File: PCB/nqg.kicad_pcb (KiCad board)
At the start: 2 copper layers, 214.3 x 81 mm, 78 parts, among them SW1 SW_PUSH, SW10 SW_PUSH, SW11 SW_PUSH, SW12 SW_PUSH, SW13 SW_PUSH, SW14 SW_PUSH, SW15 SW_PUSH, SW16 SW_PUSH, SW17 SW_PUSH, SW18 SW_PUSH, SW19 SW_PUSH, SW2 SW_PUSH, SW20 SW_PUSH, SW21 SW_PUSH, SW22 SW_PUSH, SW23 SW_PUSH, SW24 SW_PUSH, SW25 SW_PUSH, SW26 SW_PUSH, SW27 SW_PUSH, SW28 SW_PUSH, SW29 SW_PUSH, SW3 SW_PUSH, SW30 SW_PUSH, SW31 SW_PUSH, SW32 SW_PUSH, SW33 SW_PUSH, SW34 SW_PUSH, SW35 SW_PUSH, SW36 SW_PUSH, SW37 SW_PUSH, SW38 SW_PUSH, SW39 SW_PUSH, SW4 SW_PUSH, SW40 SW_PUSH, SW5 SW_PUSH, SW6 SW_PUSH, SW7 SW_PUSH, SW8 SW_PUSH, SW9 SW_PUSH, U1 ProMicro

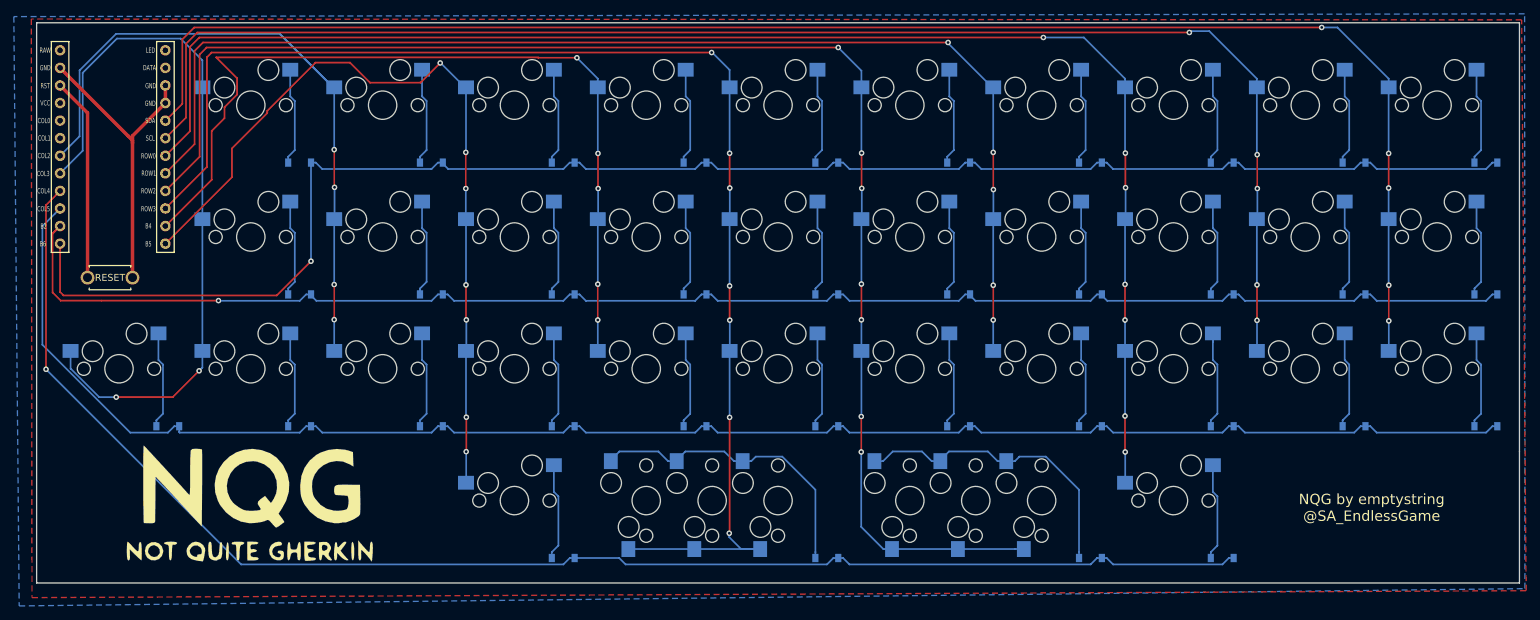
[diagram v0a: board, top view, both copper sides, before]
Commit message: added mounting holes
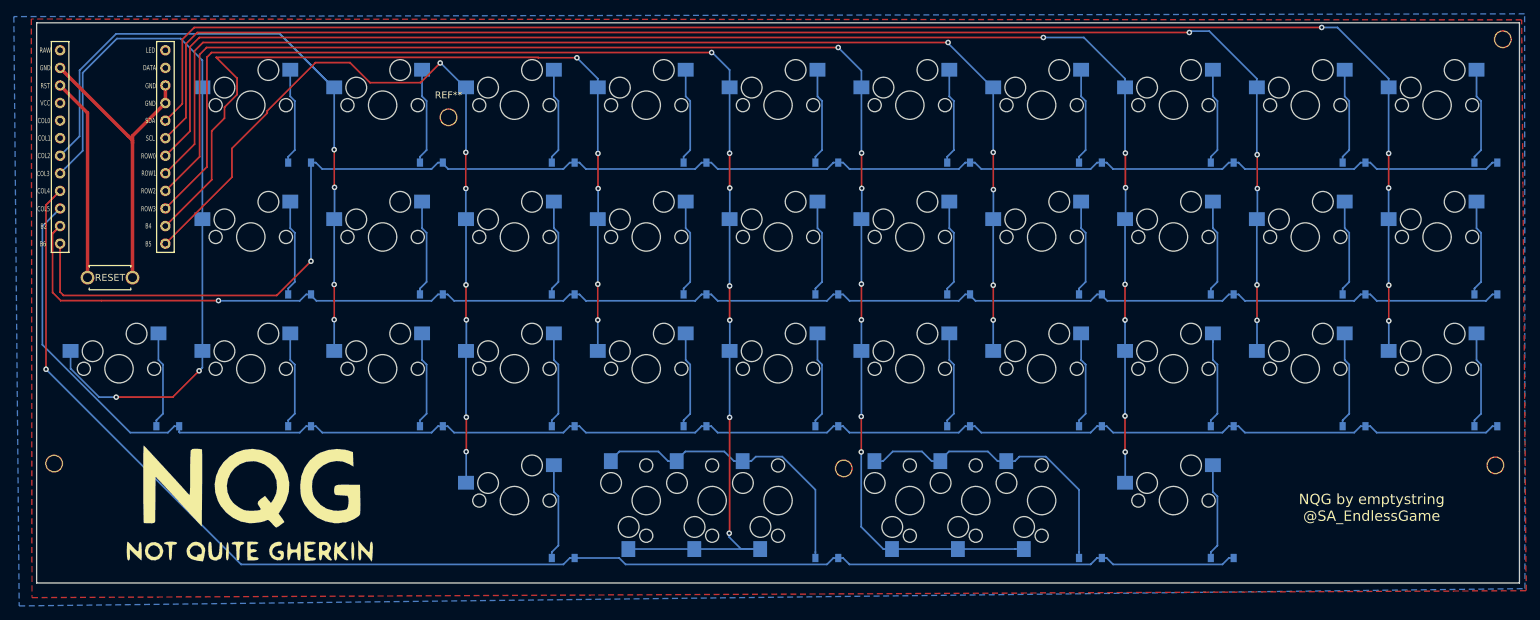
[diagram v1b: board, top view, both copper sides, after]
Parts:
- added ?: MountingHole_2.2mm_M2_Pad, MountingHole:MountingHole_2.2mm_M2_Pad, F.Cu at (143.0, 185.2)
- added ?: MountingHole_2.2mm_M2_Pad, MountingHole:MountingHole_2.2mm_M2_Pad, F.Cu at (351.3, 185.4)
- added ?: MountingHole_2.2mm_M2_Pad, MountingHole:MountingHole_2.2mm_M2_Pad, F.Cu at (257.1, 185.8)
- added ?: MountingHole_2.2mm_M2_Pad, MountingHole:MountingHole_2.2mm_M2_Pad, F.Cu at (352.4, 123.8)
- added REF**: MountingHole_2.2mm_M2_Pad, MountingHole:MountingHole_2.2mm_M2_Pad, F.Cu at (200.0, 135.1)
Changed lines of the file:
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@@
     (tracks 653)
     (zones 0)
-    (modules 78)
+    (modules 83)
     (nets 58)
   )
@@
     (mod_text_size 1 1)
     (mod_text_width 0.15)
-    (pad_size 1.524 1.524)
-    (pad_drill 0.762)
+    (pad_size 2.6 2.6)
+    (pad_drill 2.2)
     (pad_to_mask_clearance 0.051)
     (solder_mask_min_width 0.25)
@@
       (xy 17.963182 -1.693333) (xy 18.457333 -1.693333) (xy 18.457333 -4.741333)) (layer B.SilkS) (width 0.01))
   )
+  (module MountingHole:MountingHole_2.2mm_M2_Pad (layer F.Cu)
+    (at 143.025 185.15)
+    (descr "Mounting Hole 2.2mm, M2")
+    (tags "mounting hole 2.2mm m2")
+    (attr virtual)
+    (fp_text reference "" (at 0 -3.2) (layer F.SilkS)
+      (effects (font (size 1 1) (thickness 0.15)))
+    )
+    (fp_text value MountingHole_2.2mm_M2_Pad (at 0 3.2) (layer F.Fab)
+      (effects (font (size 1 1) (thickness 0.15)))
+    )
+    (fp_circle (center 0 0) (end 2.45 0) (layer F.CrtYd) (width 0.05))
+    (fp_circle (center 0 0) (end 2.2 0) (layer Cmts.User) (width 0.15))
+    (fp_text user %R (at 0.3 0) (layer F.Fab)
+      (effects (font (size 1 1) (thickness 0.15)))
+    )
+    (pad 1 thru_hole circle (at 0 0) (size 2.6 2.6) (drill 2.2) (layers *.Cu *.Mask))
+  )
+  (module MountingHole:MountingHole_2.2mm_M2_Pad (layer F.Cu)
+    (at 351.325 185.4)
+    (descr "Mounting Hole 2.2mm, M2")
+    (tags "mounting hole 2.2mm m2")
+    (attr virtual)
+    (fp_text reference "" (at 0 -3.2) (layer F.SilkS)
+      (effects (font (size 1 1) (thickness 0.15)))
+    )
+    (fp_text value MountingHole_2.2mm_M2_Pad (at 0 3.2) (layer F.Fab)
+      (effects (font (size 1 1) (thickness 0.15)))
+    )
+    (fp_circle (center 0 0) (end 2.45 0) (layer F.CrtYd) (width 0.05))
+    (fp_circle (center 0 0) (end 2.2 0) (layer Cmts.User) (width 0.15))
+    (fp_text user %R (at 0.3 0) (layer F.Fab)
+      (effects (font (size 1 1) (thickness 0.15)))
+    )
+    (pad 1 thru_hole circle (at 0 0) (size 2.6 2.6) (drill 2.2) (layers *.Cu *.Mask))
+  )
+  (module MountingHole:MountingHole_2.2mm_M2_Pad (layer F.Cu)
+    (at 257.15 185.85)
+    (descr "Mounting Hole 2.2mm, M2")
+    (tags "mounting hole 2.2mm m2")
+    (attr virtual)
+    (fp_text reference "" (at 0 -3.2) (layer F.SilkS)
+      (effects (font (size 1 1) (thickness 0.15)))
+    )
+    (fp_text value MountingHole_2.2mm_M2_Pad (at 0 3.2) (layer F.Fab)
+      (effects (font (size 1 1) (thickness 0.15)))
+    )
+    (fp_circle (center 0 0) (end 2.45 0) (layer F.CrtYd) (width 0.05))
+    (fp_circle (center 0 0) (end 2.2 0) (layer Cmts.User) (width 0.15))
+    (fp_text user %R (at 0.3 0) (layer F.Fab)
+      (effects (font (size 1 1) (thickness 0.15)))
+    )
+    (pad 1 thru_hole circle (at 0 0) (size 2.6 2.6) (drill 2.2) (layers *.Cu *.Mask))
+  )
+  (module MountingHole:MountingHole_2.2mm_M2_Pad (layer F.Cu)
+    (at 352.4 123.825)
+    (descr "Mounting Hole 2.2mm, M2")
+    (tags "mounting hole 2.2mm m2")
+    (attr virtual)
+    (fp_text reference "" (at 0 -3.2) (layer F.SilkS)
+      (effects (font (size 1 1) (thickness 0.15)))
+    )
+    (fp_text value MountingHole_2.2mm_M2_Pad (at 0 3.2) (layer F.Fab)
+      (effects (font (size 1 1) (thickness 0.15)))
+    )
+    (fp_circle (center 0 0) (end 2.45 0) (layer F.CrtYd) (width 0.05))
+    (fp_circle (center 0 0) (end 2.2 0) (layer Cmts.User) (width 0.15))
+    (fp_text user %R (at 0.3 0) (layer F.Fab)
+      (effects (font (size 1 1) (thickness 0.15)))
+    )
+    (pad 1 thru_hole circle (at 0 0) (size 2.6 2.6) (drill 2.2) (layers *.Cu *.Mask))
+  )
+  (module MountingHole:MountingHole_2.2mm_M2_Pad (layer F.Cu)
+    (at 200.025 135.1)
+    (descr "Mounting Hole 2.2mm, M2")
+    (tags "mounting hole 2.2mm m2")
+    (attr virtual)
+    (fp_text reference REF** (at 0 -3.2) (layer F.SilkS)
+      (effects (font (size 1 1) (thickness 0.15)))
+    )
+    (fp_text value MountingHole_2.2mm_M2_Pad (at 0 3.2) (layer F.Fab)
+      (effects (font (size 1 1) (thickness 0.15)))
+    )
+    (fp_circle (center 0 0) (end 2.45 0) (layer F.CrtYd) (width 0.05))
+    (fp_circle (center 0 0) (end 2.2 0) (layer Cmts.User) (width 0.15))
+    (fp_text user %R (at 0.3 0) (layer F.Fab)
+      (effects (font (size 1 1) (thickness 0.15)))
+    )
+    (pad 1 thru_hole circle (at 0 0) (size 2.6 2.6) (drill 2.2) (layers *.Cu *.Mask))
+  )
   (gr_text "NQG by emptystring\n@SA_EndlessGame" (at 333.45 191.525) (layer F.SilkS)
